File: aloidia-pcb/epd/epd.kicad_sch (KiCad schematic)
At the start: 20 parts, among them J1 FH12-30S-0.5SH(55), J2 01x08 2.54mm Pin Headers

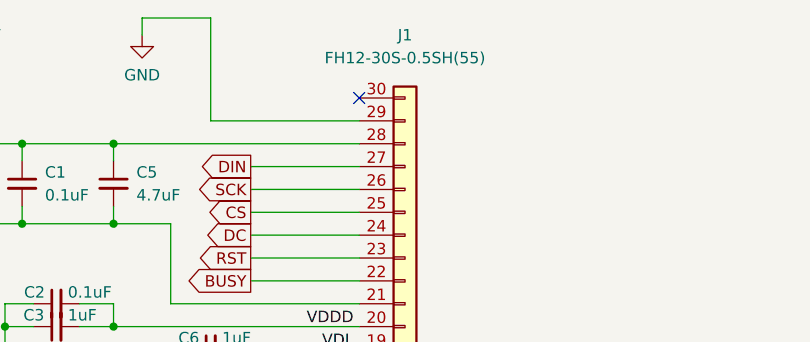
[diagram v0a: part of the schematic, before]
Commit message: Made e-ink display shorter
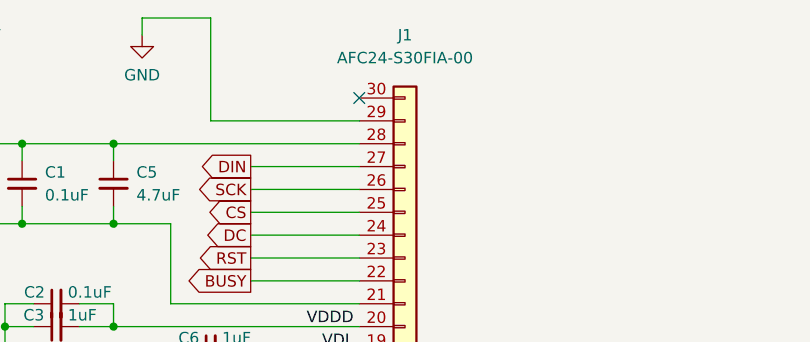
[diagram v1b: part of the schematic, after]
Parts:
- J1: value FH12-30S-0.5SH(55) -> AFC24-S30FIA-00; Manufacturer ref FH12-30S-0.5SH(55) -> AFC24-S30FIA-00; Mouser ref 798-FH12-30S-0.5SH55 -> (none)
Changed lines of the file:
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@@
     (in_bom yes) (on_board yes) (fields_autoplaced)
     (property "Reference" "J1" (id 0) (at 116.205 52.705 0))
-    (property "Value" "FH12-30S-0.5SH(55)" (id 1) (at 116.205 55.245 0))
+    (property "Value" "AFC24-S30FIA-00" (id 1) (at 116.205 55.245 0))
     (property "Footprint" "0_various:JUSHUO AFC24-S30FIC-00" (id 2) (at 116.205 97.79 0)
       (effects (font (size 1.27 1.27)) hide)
     )
-    (property "Datasheet" "https://www.mouser.ch/datasheet/2/185/FH12_30S_0_5SH_55__CL0586_0525_1_55_2DDrawing_0000-1614880.pdf" (id 3) (at 116.205 97.79 0)
-      (effects (font (size 1.27 1.27)) hide)
-    )
-    (property "Manufacturer ref" "FH12-30S-0.5SH(55)" (id 4) (at 116.205 97.79 0)
-      (effects (font (size 1.27 1.27)) hide)
-    )
-    (property "Mouser ref" "798-FH12-30S-0.5SH55" (id 5) (at 116.205 97.79 0)
+    (property "Datasheet" "https://datasheet.lcsc.com/lcsc/1811021329_JUSHUO-AFC24-S30FIA-00_C262685.pdf" (id 3) (at 116.205 97.79 0)
+      (effects (font (size 1.27 1.27)) hide)
+    )
+    (property "Manufacturer ref" "AFC24-S30FIA-00" (id 4) (at 116.205 97.79 0)
       (effects (font (size 1.27 1.27)) hide)
     )
@@
     )
     (path "/56d8783b-8482-4fc3-a815-7fb0e0a20be0"
-      (reference "J1") (unit 1) (value "FH12-30S-0.5SH(55)") (footprint "0_various:JUSHUO AFC24-S30FIC-00")
+      (reference "J1") (unit 1) (value "AFC24-S30FIA-00") (footprint "0_various:JUSHUO AFC24-S30FIC-00")
     )
     (path "/872f375f-df9c-43e7-a4aa-038b245980e0"
